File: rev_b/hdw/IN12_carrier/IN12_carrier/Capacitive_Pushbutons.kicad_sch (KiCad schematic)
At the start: 65 parts, among them U2203 74LVC1G17

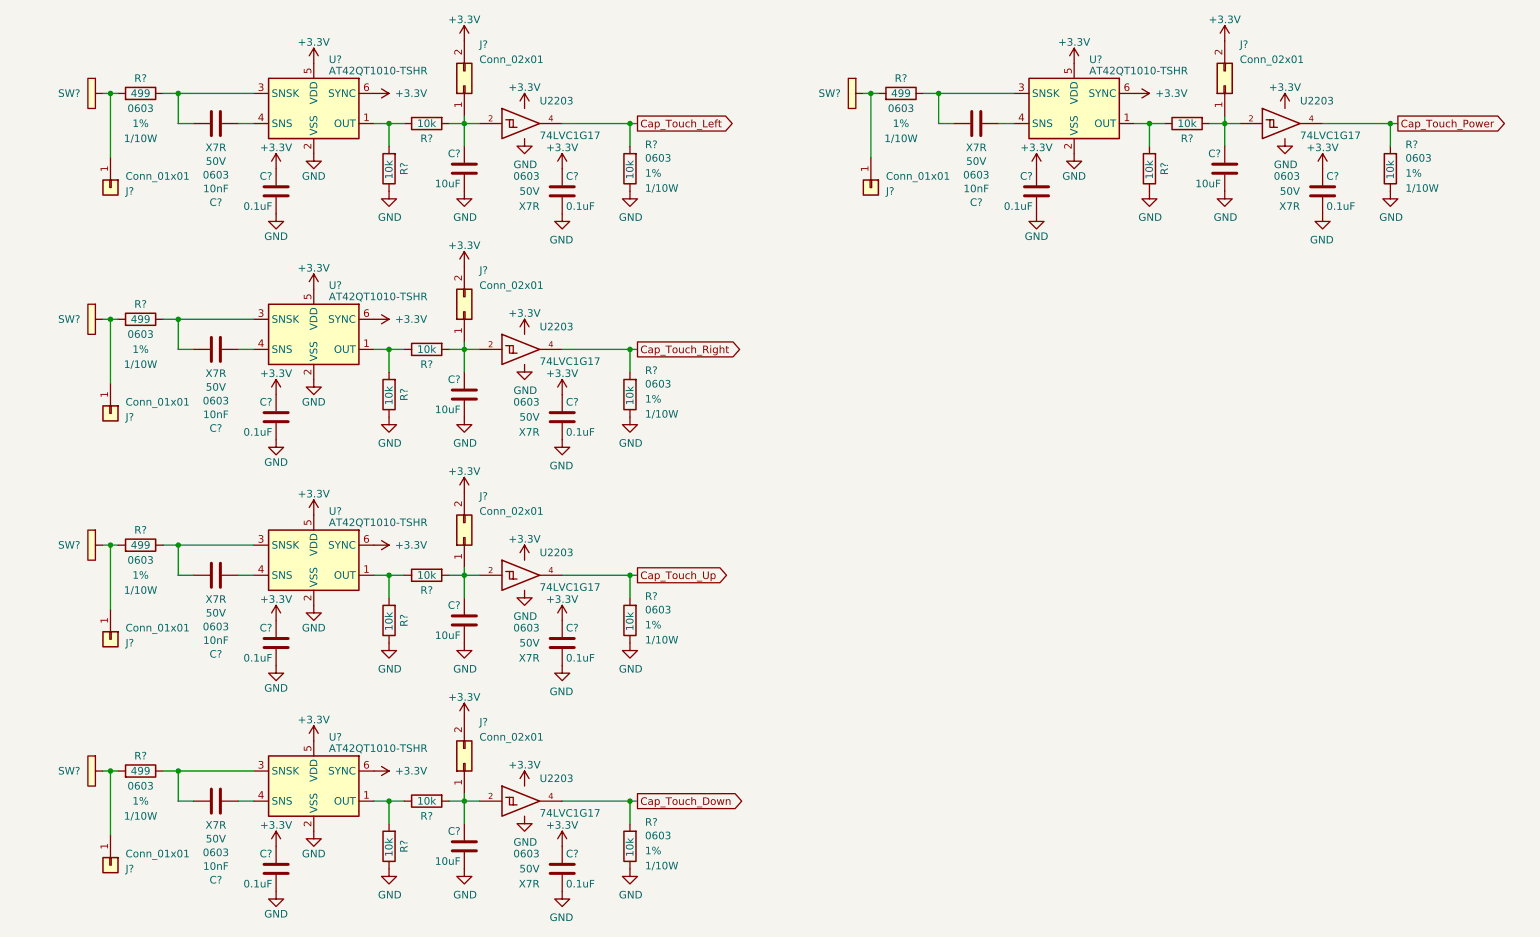
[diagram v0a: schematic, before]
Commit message: annotated, started arranging parts for IN12 carrier
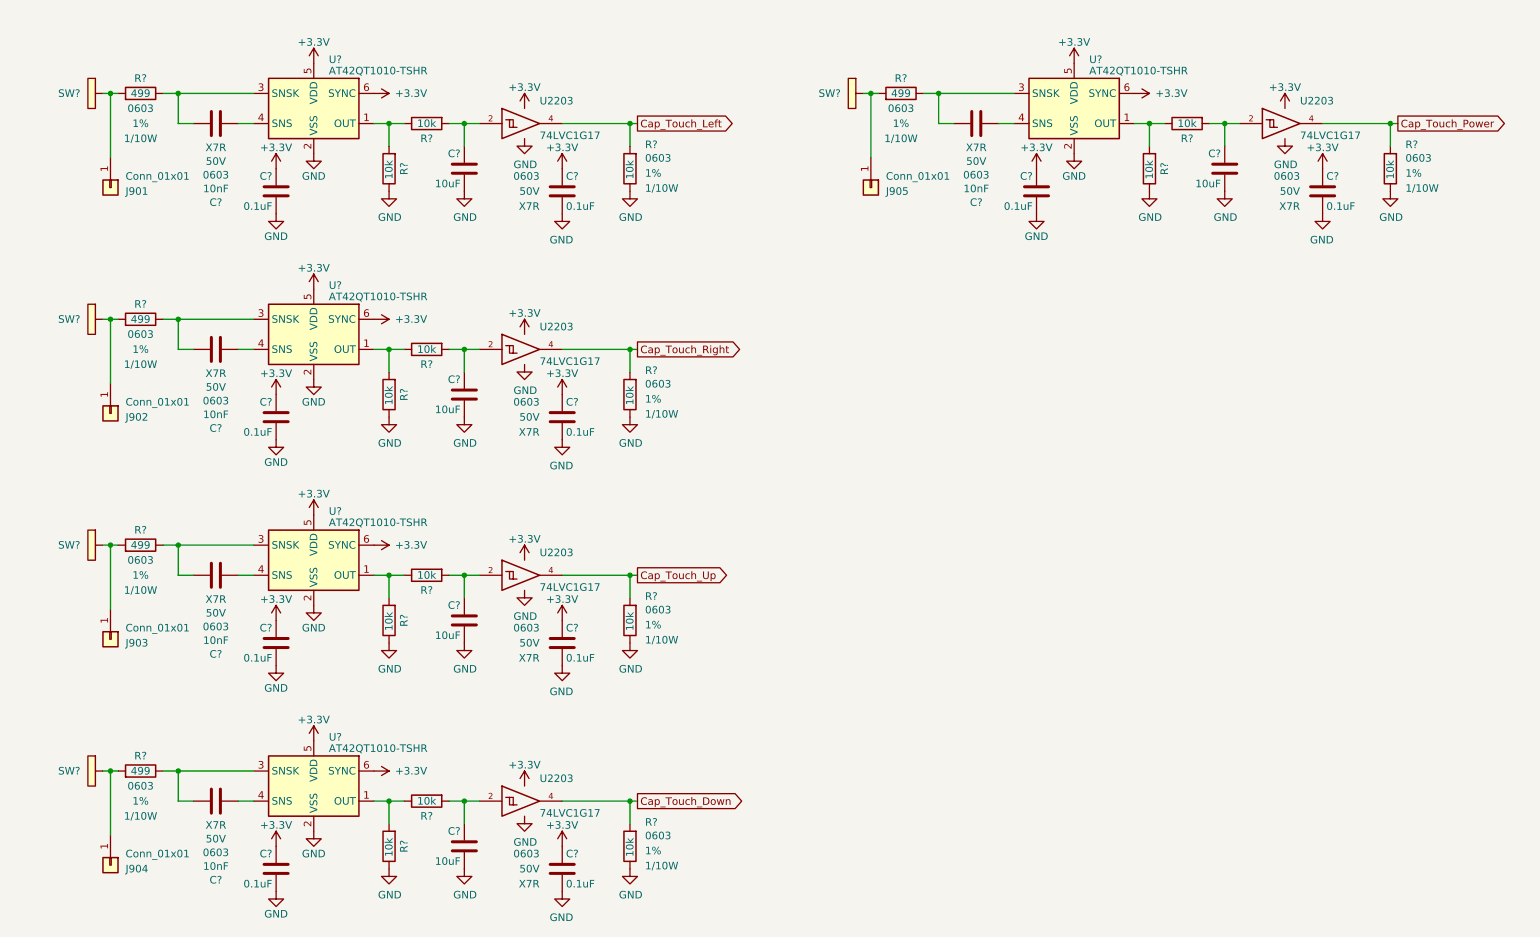
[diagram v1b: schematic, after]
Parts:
- removed J? (x5): Conn_02x01, symbol Connector_Generic:Conn_02x01
- gave numbers to parts that had none: 5

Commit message: lots of placement progress on IN12 carrier board
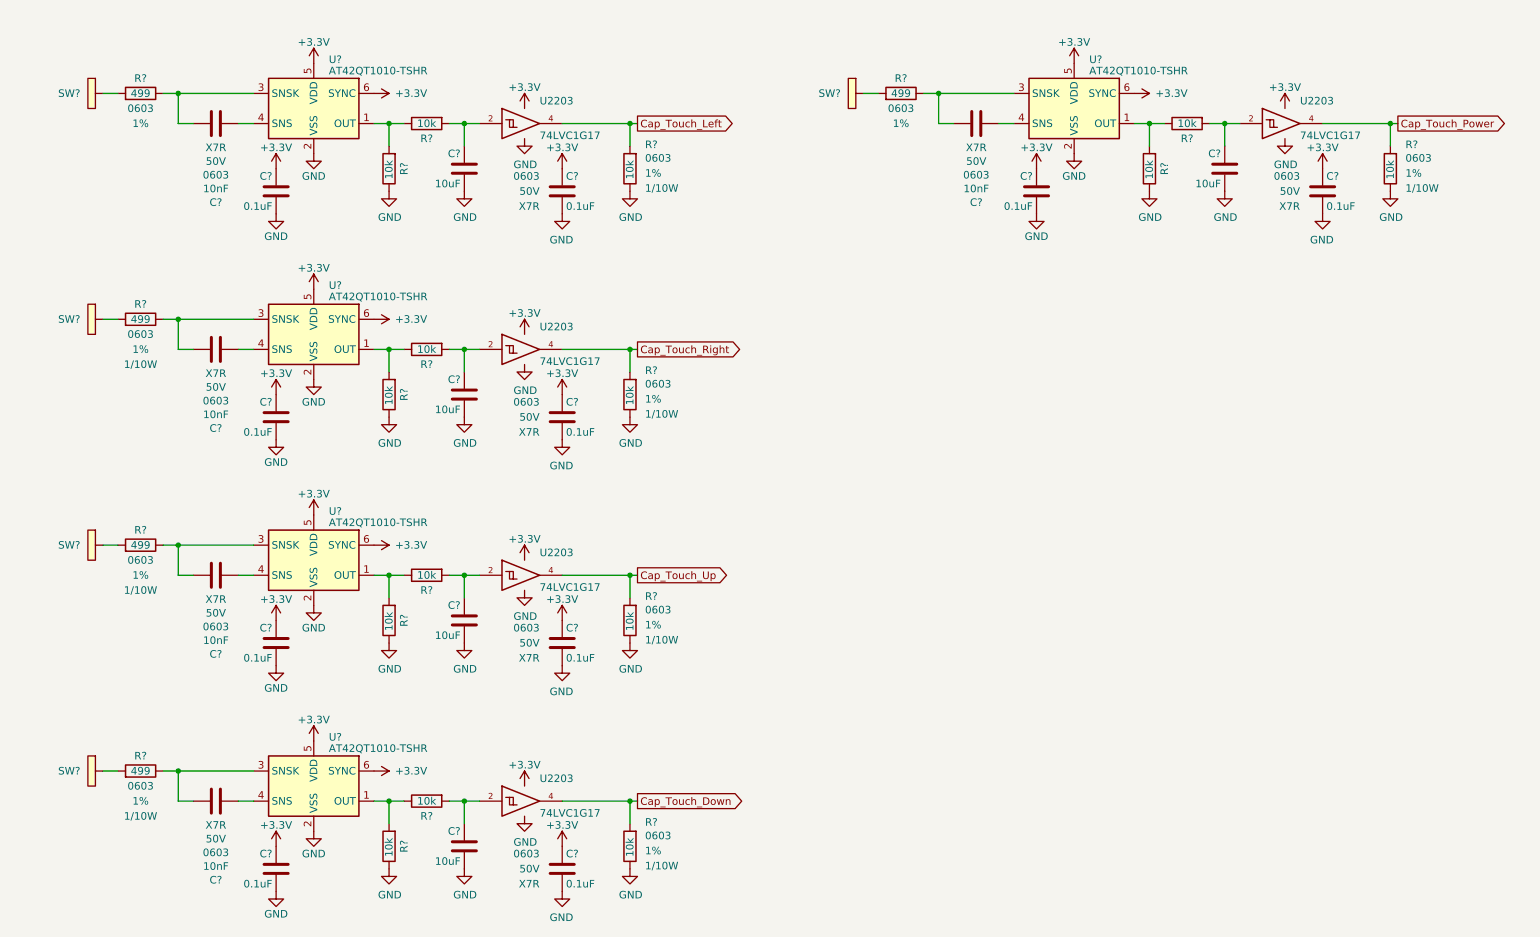
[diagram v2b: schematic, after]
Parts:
- removed J901, J902, J903, J904, J905: Conn_01x01, symbol Connector_Generic:Conn_01x01
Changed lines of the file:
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@@
     (company "Drew Maatman")
   )
-  (junction (at 29.21 102.87) (diameter 0) (color 0 0 0 0)
-  )
   (junction (at 88.9 107.95) (diameter 0) (color 0 0 0 0)
   )
   (junction (at 168.91 26.67) (diameter 0) (color 0 0 0 0)
   )
-  (junction (at 29.21 64.77) (diameter 0) (color 0 0 0 0)
-  )
   (junction (at 76.2 146.05) (diameter 0) (color 0 0 0 0)
   )
@@
   (junction (at 88.9 146.05) (diameter 0) (color 0 0 0 0)
   )
-  (junction (at 29.21 140.97) (diameter 0) (color 0 0 0 0)
-  )
   (junction (at 116.84 146.05) (diameter 0) (color 0 0 0 0)
   )
@@
   (junction (at 40.64 102.87) (diameter 0) (color 0 0 0 0)
   )
-  (junction (at 29.21 26.67) (diameter 0) (color 0 0 0 0)
-  )
-  (junction (at 157.48 26.67) (diameter 0) (color 0 0 0 0)
-  )
   (junction (at 40.64 26.67) (diameter 0) (color 0 0 0 0)
   )
@@
     (stroke (width 0) (type default))
   )
-  (wire (pts (xy 29.21 102.87) (xy 29.21 113.665))
-    (stroke (width 0) (type default))
-  )
   (wire (pts (xy 50.8 69.85) (xy 53.34 69.85))
     (stroke (width 0) (type default))
@@
     (stroke (width 0) (type default))
   )
-  (wire (pts (xy 27.94 26.67) (xy 29.21 26.67))
+  (wire (pts (xy 27.94 26.67) (xy 30.48 26.67))
     (stroke (width 0) (type default))
   )
@@
     (stroke (width 0) (type default))
   )
-  (wire (pts (xy 156.21 26.67) (xy 157.48 26.67))
+  (wire (pts (xy 156.21 26.67) (xy 158.75 26.67))
     (stroke (width 0) (type default))
   )
@@
     (stroke (width 0) (type default))
   )
-  (wire (pts (xy 157.48 26.67) (xy 158.75 26.67))
-    (stroke (width 0) (type default))
-  )
   (wire (pts (xy 118.11 146.05) (xy 116.84 146.05))
     (stroke (width 0) (type default))
@@
     (stroke (width 0) (type default))
   )
-  (wire (pts (xy 29.21 26.67) (xy 30.48 26.67))
-    (stroke (width 0) (type default))
-  )
   (wire (pts (xy 168.91 31.75) (xy 168.91 26.67))
     (stroke (width 0) (type default))
@@
     (stroke (width 0) (type default))
   )
-  (wire (pts (xy 29.21 140.97) (xy 29.21 151.765))
-    (stroke (width 0) (type default))
-  )
   (wire (pts (xy 116.84 149.86) (xy 116.84 146.05))
     (stroke (width 0) (type default))
   )
-  (wire (pts (xy 27.94 102.87) (xy 29.21 102.87))
+  (wire (pts (xy 27.94 102.87) (xy 30.48 102.87))
     (stroke (width 0) (type default))
   )
@@
     (stroke (width 0) (type default))
   )
-  (wire (pts (xy 29.21 64.77) (xy 30.48 64.77))
+  (wire (pts (xy 27.94 64.77) (xy 30.48 64.77))
     (stroke (width 0) (type default))
   )
@@
     (stroke (width 0) (type default))
   )
-  (wire (pts (xy 29.21 26.67) (xy 29.21 37.465))
-    (stroke (width 0) (type default))
-  )
   (wire (pts (xy 217.17 31.75) (xy 214.63 31.75))
     (stroke (width 0) (type default))
   )
-  (wire (pts (xy 157.48 26.67) (xy 157.48 37.465))
-    (stroke (width 0) (type default))
-  )
   (wire (pts (xy 50.8 107.95) (xy 53.34 107.95))
     (stroke (width 0) (type default))
@@
     (stroke (width 0) (type default))
   )
-  (wire (pts (xy 29.21 102.87) (xy 30.48 102.87))
-    (stroke (width 0) (type default))
-  )
   (wire (pts (xy 88.9 73.66) (xy 88.9 69.85))
     (stroke (width 0) (type default))
@@
     (stroke (width 0) (type default))
   )
-  (wire (pts (xy 27.94 140.97) (xy 29.21 140.97))
+  (wire (pts (xy 27.94 140.97) (xy 30.48 140.97))
     (stroke (width 0) (type default))
   )
@@
     (stroke (width 0) (type default))
   )
-  (wire (pts (xy 29.21 140.97) (xy 30.48 140.97))
-    (stroke (width 0) (type default))
-  )
   (wire (pts (xy 76.2 111.76) (xy 76.2 107.95))
     (stroke (width 0) (type default))
   )
-  (wire (pts (xy 27.94 64.77) (xy 29.21 64.77))
-    (stroke (width 0) (type default))
-  )
-  (wire (pts (xy 29.21 64.77) (xy 29.21 75.565))
-    (stroke (width 0) (type default))
-  )
   (wire (pts (xy 76.2 73.66) (xy 76.2 69.85))
     (stroke (width 0) (type default))
@@
     )
     (property "Wattage" "1/10W" (at 34.29 34.29 90)
-      (effects (font (size 1.27 1.27)))
+      (effects (font (size 1.27 1.27)) hide)
     )
     (pin "1")
@@
     )
   )
-  (symbol (lib_id "Connector_Generic:Conn_01x01") (at 29.21 156.845 270) (unit 1)
-    (in_bom yes) (on_board yes) (dnp no)
-    (property "Reference" "J904" (at 31.75 157.48 90)
-      (effects (font (size 1.27 1.27)) (justify left))
-    )
-    (property "Value" "Conn_01x01" (at 31.75 154.94 90)
-      (effects (font (size 1.27 1.27)) (justify left))
-    )
-    (property "Footprint" "" (at 29.21 156.845 0)
-      (effects (font (size 1.27 1.27)) hide)
-    )
-    (property "Datasheet" "~" (at 29.21 156.845 0)
-      (effects (font (size 1.27 1.27)) hide)
-    )
-    (pin "1")
-    (instances
-      (project "IN12_carrier"
-        (path "/c4d83a5b-e6ae-4326-9df5-0c4ac01f7d8c/c2a3d93b-f6d3-42f3-baff-03db67a5d3d0"
-          (reference "J904") (unit 1)
-        )
-      )
-    )
-  )
   (symbol (lib_id "Sensor_Touch:AT42QT1010-TSHR") (at 63.5 105.41 0) (mirror y) (unit 1)
     (in_bom yes) (on_board yes) (dnp no)
@@
     )
   )
-  (symbol (lib_id "Connector_Generic:Conn_01x01") (at 29.21 42.545 270) (unit 1)
-    (in_bom yes) (on_board yes) (dnp no)
-    (property "Reference" "J901" (at 31.75 43.18 90)
-      (effects (font (size 1.27 1.27)) (justify left))
-    )
-    (property "Value" "Conn_01x01" (at 31.75 40.64 90)
-      (effects (font (size 1.27 1.27)) (justify left))
-    )
-    (property "Footprint" "" (at 29.21 42.545 0)
-      (effects (font (size 1.27 1.27)) hide)
-    )
-    (property "Datasheet" "~" (at 29.21 42.545 0)
-      (effects (font (size 1.27 1.27)) hide)
-    )
-    (pin "1")
-    (instances
-      (project "IN12_carrier"
-        (path "/c4d83a5b-e6ae-4326-9df5-0c4ac01f7d8c/c2a3d93b-f6d3-42f3-baff-03db67a5d3d0"
-          (reference "J901") (unit 1)
-        )
-      )
-    )
-  )
   (symbol (lib_id "Analog_Clock-rescue:+3.3V-power") (at 73.66 26.67 270) (unit 1)
     (in_bom yes) (on_board yes) (dnp no)
@@
     )
   )
-  (symbol (lib_id "Connector_Generic:Conn_01x01") (at 29.21 118.745 270) (unit 1)
-    (in_bom yes) (on_board yes) (dnp no)
-    (property "Reference" "J903" (at 31.75 119.38 90)
-      (effects (font (size 1.27 1.27)) (justify left))
-    )
-    (property "Value" "Conn_01x01" (at 31.75 116.84 90)
-      (effects (font (size 1.27 1.27)) (justify left))
-    )
-    (property "Footprint" "" (at 29.21 118.745 0)
-      (effects (font (size 1.27 1.27)) hide)
-    )
-    (property "Datasheet" "~" (at 29.21 118.745 0)
-      (effects (font (size 1.27 1.27)) hide)
-    )
-    (pin "1")
-    (instances
-      (project "IN12_carrier"
-        (path "/c4d83a5b-e6ae-4326-9df5-0c4ac01f7d8c/c2a3d93b-f6d3-42f3-baff-03db67a5d3d0"
-          (reference "J903") (unit 1)
-        )
-      )
-    )
-  )
   (symbol (lib_id "Custom_Library:C_Custom") (at 217.17 39.37 0) (mirror y) (unit 1)
     (in_bom yes) (on_board yes) (dnp no)
@@
     )
   )
-  (symbol (lib_id "Connector_Generic:Conn_01x01") (at 29.21 80.645 270) (unit 1)
-    (in_bom yes) (on_board yes) (dnp no)
-    (property "Reference" "J902" (at 31.75 81.28 90)
-      (effects (font (size 1.27 1.27)) (justify left))
-    )
-    (property "Value" "Conn_01x01" (at 31.75 78.74 90)
-      (effects (font (size 1.27 1.27)) (justify left))
-    )
-    (property "Footprint" "" (at 29.21 80.645 0)
-      (effects (font (size 1.27 1.27)) hide)
-    )
-    (property "Datasheet" "~" (at 29.21 80.645 0)
-      (effects (font (size 1.27 1.27)) hide)
-    )
-    (pin "1")
-    (instances
-      (project "IN12_carrier"
-        (path "/c4d83a5b-e6ae-4326-9df5-0c4ac01f7d8c/c2a3d93b-f6d3-42f3-baff-03db67a5d3d0"
-          (reference "J902") (unit 1)
-        )
-      )
-    )
-  )
   (symbol (lib_id "power:GND") (at 76.2 119.38 0) (unit 1)
     (in_bom yes) (on_board yes) (dnp no)
@@
     )
   )
-  (symbol (lib_id "Connector_Generic:Conn_01x01") (at 157.48 42.545 270) (unit 1)
-    (in_bom yes) (on_board yes) (dnp no)
-    (property "Reference" "J905" (at 160.02 43.18 90)
-      (effects (font (size 1.27 1.27)) (justify left))
-    )
-    (property "Value" "Conn_01x01" (at 160.02 40.64 90)
-      (effects (font (size 1.27 1.27)) (justify left))
-    )
-    (property "Footprint" "" (at 157.48 42.545 0)
-      (effects (font (size 1.27 1.27)) hide)
-    )
-    (property "Datasheet" "~" (at 157.48 42.545 0)
-      (effects (font (size 1.27 1.27)) hide)
-    )
-    (pin "1")
-    (instances
-      (project "IN12_carrier"
-        (path "/c4d83a5b-e6ae-4326-9df5-0c4ac01f7d8c/c2a3d93b-f6d3-42f3-baff-03db67a5d3d0"
-          (reference "J905") (unit 1)
-        )
-      )
-    )
-  )
   (symbol (lib_id "Custom_Library:R_Custom") (at 162.56 26.67 90) (mirror x) (unit 1)
     (in_bom yes) (on_board yes) (dnp no)
@@
     )
     (property "Wattage" "1/10W" (at 162.56 34.29 90)
-      (effects (font (size 1.27 1.27)))
+      (effects (font (size 1.27 1.27)) hide)
     )
     (pin "1")

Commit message: lots more IN12 carrier placement
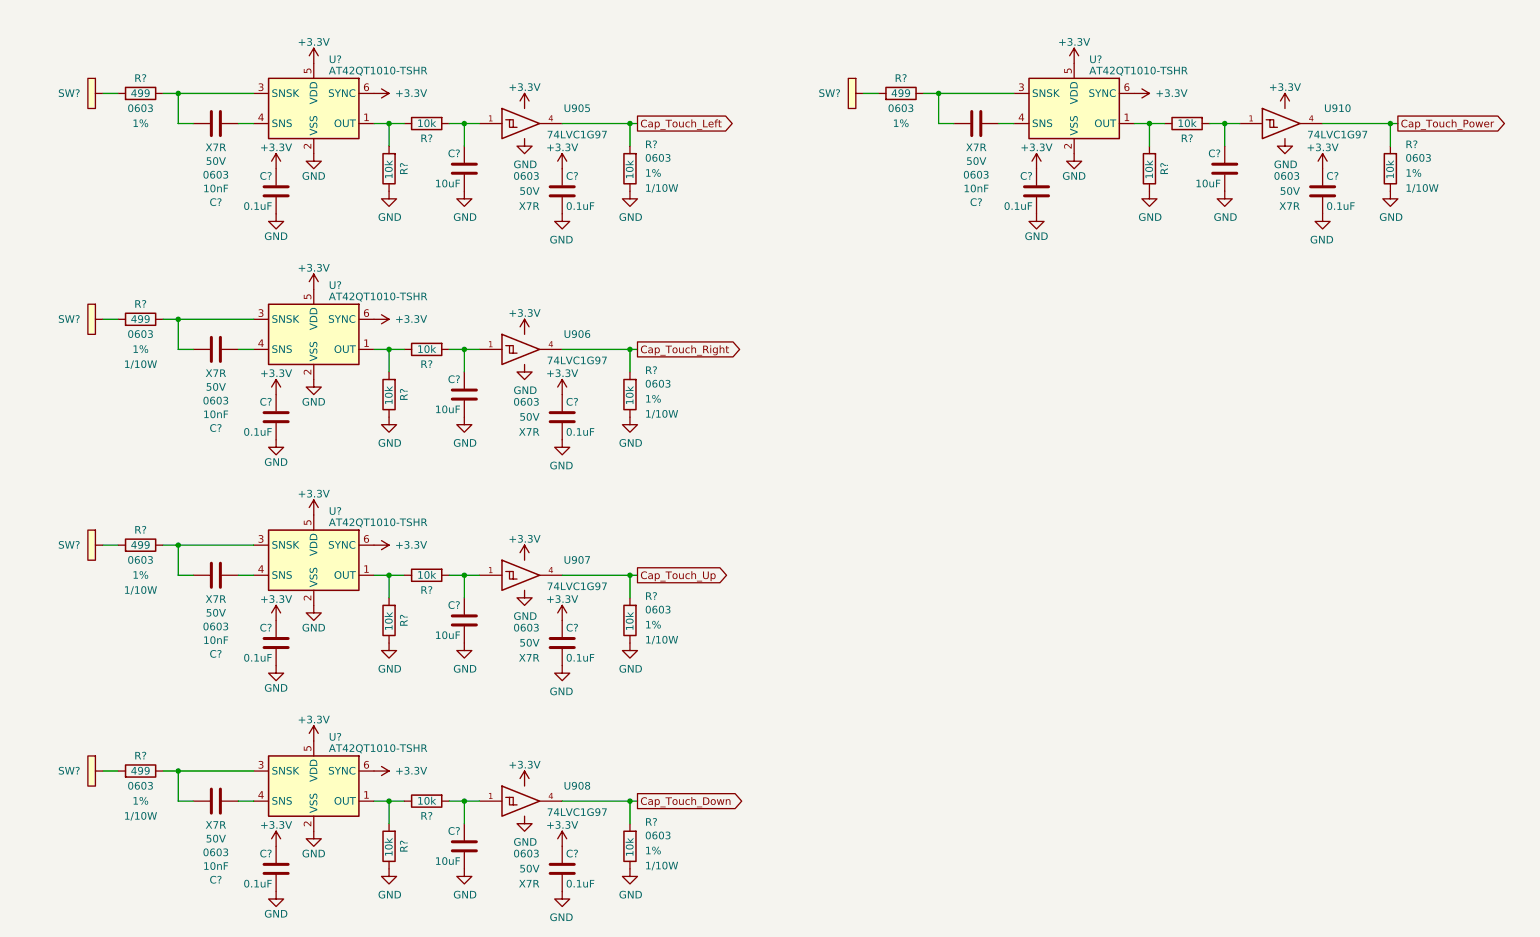
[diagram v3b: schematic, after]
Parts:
- removed U2203 (x5): 74LVC1G17, TO_SOT_Packages_SMD:SOT-353_SC-70-5, symbol Custom_Library:74LVC1G17_Power
- added U905, U906, U907, U908, U910: 74LVC1G97, Package_TO_SOT_SMD:SOT-363_SC-70-6, symbol Custom Library:74LVC1G97_Power_BUF
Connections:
- net +3V3: now also U905.5 (VCC), U906.5 (VCC), U907.5 (VCC), U908.5 (VCC), U910.5 (VCC)
- net Cap_Touch_Down: now also U908.4
- net Cap_Touch_Left: now also U905.4
- net Cap_Touch_Power: now also U910.4
- net Cap_Touch_Right: now also U906.4
- net Cap_Touch_Up: now also U907.4
- net GND: now also U905.2 (GND), U905.3 (GND), U905.6 (GND), U906.2 (GND), U906.3 (GND), U906.6 (GND), U907.2 (GND), U907.3 (GND), U907.6 (GND), U908.2 (GND), U908.3 (GND), U908.6 (GND), U910.2 (GND), U910.3 (GND), U910.6 (GND)
- net at C?.1, R?.1: now also U906.1
- net at C?.1, R?.1: now also U907.1
- net at C?.1, R?.1: now also U908.1
- net at C?.1, R?.1: now also U910.1
- net at C?.1, R?.1: now also U905.1
